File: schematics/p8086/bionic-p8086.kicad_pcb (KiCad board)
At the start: 2 copper layers, 25.4 x 68.6 mm, 8 parts, among them J1 Bionic-P135, J2 Bionic-P245, U1 P8086, U2 11AA010-I/TT

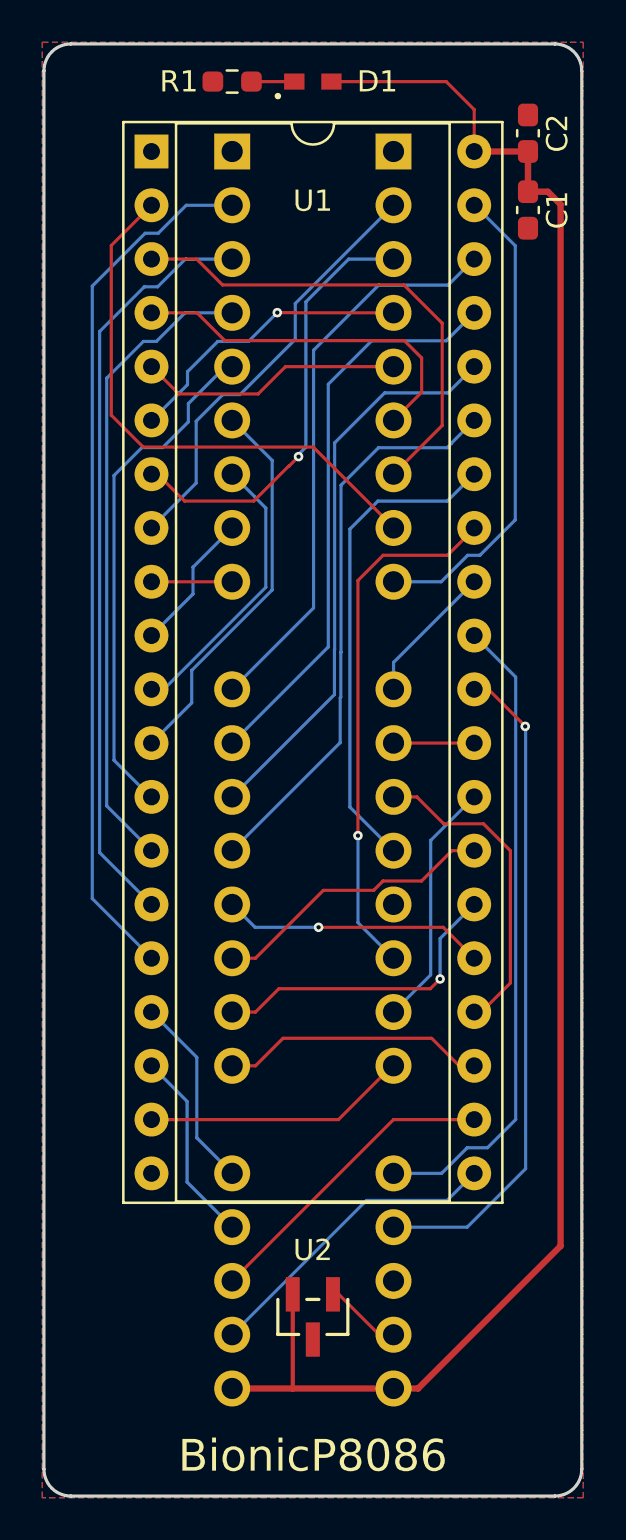
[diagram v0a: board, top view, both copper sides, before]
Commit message: [p8086] Clean up the P8086 tracks and regenerate Gerbers
Pad-exit stubs merged into straight and 45-degree runs, every track
ending on its pad centre; C1/C2 labels aligned. Re-exported the
schematic PDF.
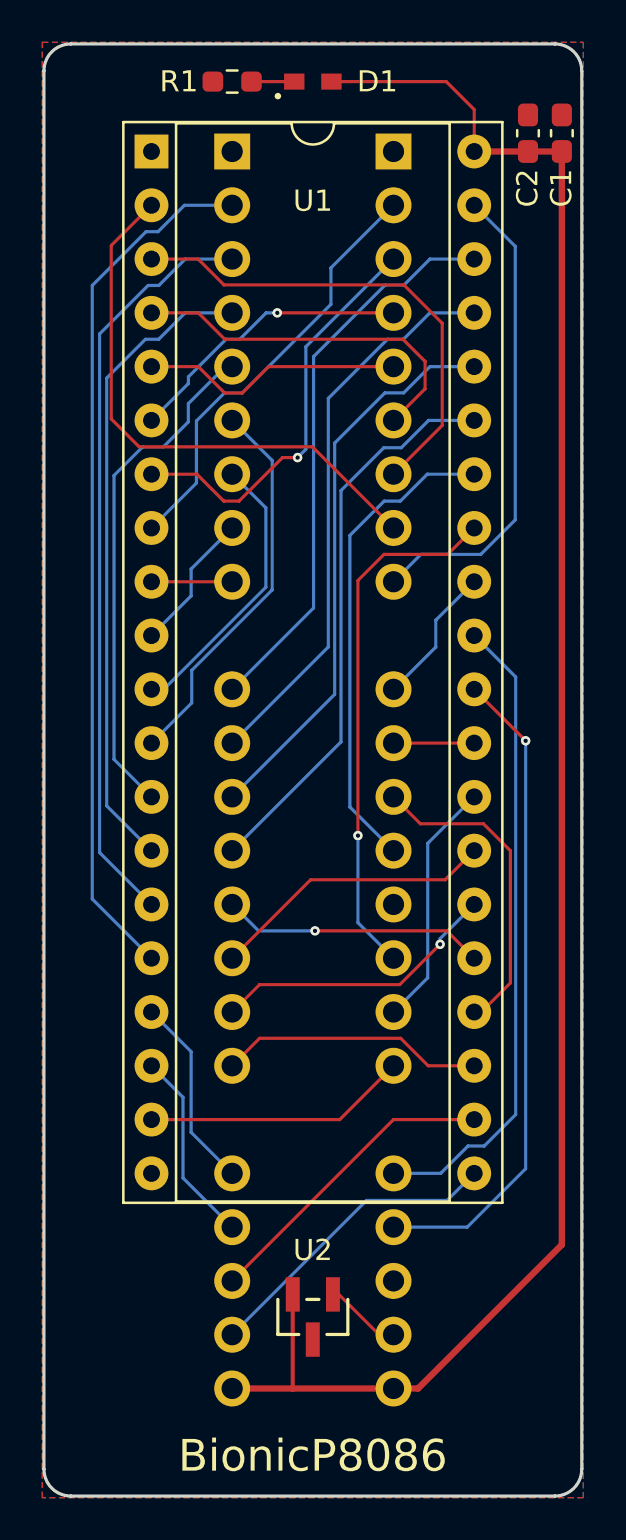
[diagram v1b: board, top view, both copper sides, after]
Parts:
- moved C1 3.96 mm to (125.5, 74.2), turned to 90 degrees
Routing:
- net AD9: track 20.8 -> 19.5 mm
- net ~{DEN}: track 14.7 -> 13.7 mm
